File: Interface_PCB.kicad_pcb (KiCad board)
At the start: 2 copper layers, 46.5 x 47.9 mm, 48 parts, among them IC1 STM32L412RBT6P, J1 Conn_01x04, J2 Conn_01x04, J3 Conn_01x04, J4 Conn_01x04, J5 AVR-JTAG-10, J6 Micro_SD_Card, J7 USB_B, J8 Conn_01x02_Male, U1 AMS1117-3.3, Y1 Crystal, Y2 Crystal

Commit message: Design 5.0
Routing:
- net LSE_OUT: track 13.5 -> 15.1 mm, vias 2 -> 0
- net GND: track 86.6 -> 87.6 mm
- net LSE_IN: track 9.17 -> 8.66 mm
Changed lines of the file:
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@@
     (property "Sheetname" "")
     (attr smd)
-    (fp_text reference "Cl2" (at -1.5702 1.0562 180) (layer "F.SilkS")
+    (fp_text reference "Cl2" (at -1.498 0.7768 180) (layer "F.SilkS")
       (effects (font (size 0.5 0.5) (thickness 0.125)))
     )
@@
   (segment (start 132.3256 111.1334) (end 131.8556 111.6034) (width 0.25) (layer "F.Cu") (net 2))
   (segment (start 126.5556 100.0236) (end 124.7756 100.0236) (width 0.25) (layer "F.Cu") (net 2))
-  (segment (start 126.7743 109.5248) (end 125.9738 109.5248) (width 0.25) (layer "F.Cu") (net 2))
-  (segment (start 125.768 96.611) (end 127.308 96.611) (width 0.25) (layer "F.Cu") (net 2))
   (segment (start 125.8502 103.5236) (end 125.8316 103.505) (width 0.25) (layer "F.Cu") (net 2))
   (segment (start 132.8674 93.8754) (end 132.7856 93.7936) (width 0.25) (layer "F.Cu") (net 2))
+  (segment (start 126.5428 96.5962) (end 126.5576 96.611) (width 0.25) (layer "F.Cu") (net 2))
   (segment (start 132.386 105.859668) (end 132.386 108.7604) (width 0.25) (layer "F.Cu") (net 2))
   (segment (start 129.898 104.7724) (end 131.5948 104.7724) (width 0.25) (layer "F.Cu") (net 2))
+  (segment (start 125.7828 96.5962) (end 125.768 96.611) (width 0.25) (layer "F.Cu") (net 2))
   (segment (start 128.4224 115.3008) (end 130.0328 113.6904) (width 0.25) (layer "F.Cu") (net 2))
-  (segment (start 125.768 96.611) (end 125.768 96.596) (width 0.25) (layer "F.Cu") (net 2))
   (segment (start 143.3056 99.5236) (end 145.2756 99.5236) (width 0.25) (layer "F.Cu") (net 2))
   (segment (start 132.7856 92.2636) (end 133.2556 91.7936) (width 0.25) (layer "F.Cu") (net 2))
@@
   (segment (start 138.9229 85.9028) (end 137.8979 85.9028) (width 0.25) (layer "F.Cu") (net 2))
   (segment (start 152.3977 92.8878) (end 152.3977 89.2302) (width 0.25) (layer "F.Cu") (net 2))
-  (segment (start 125.768 96.596) (end 126.4864 95.8776) (width 0.25) (layer "F.Cu") (net 2))
   (segment (start 152.3977 92.8878) (end 154.0764 92.8878) (width 0.25) (layer "F.Cu") (net 2))
   (segment (start 154.0764 92.8878) (end 154.4066 92.5576) (width 0.25) (layer "F.Cu") (net 2))
+  (segment (start 126.5428 96.5962) (end 125.7828 96.5962) (width 0.25) (layer "F.Cu") (net 2))
   (segment (start 138.3792 121.7676) (end 138.3556 121.744) (width 0.25) (layer "F.Cu") (net 2))
   (segment (start 132.585896 105.659772) (end 132.386 105.859668) (width 0.25) (layer "F.Cu") (net 2))
@@
   (segment (start 141.374 99.7724) (end 143.0568 99.7724) (width 0.25) (layer "F.Cu") (net 2))
   (segment (start 117.5202 117.4186) (end 117.4242 117.3226) (width 0.25) (layer "F.Cu") (net 2))
+  (segment (start 125.3744 107.7696) (end 125.3744 108.9254) (width 0.25) (layer "F.Cu") (net 2))
   (segment (start 130.9588 113.6904) (end 131.8556 112.7936) (width 0.25) (layer "F.Cu") (net 2))
   (segment (start 132.386 98.1468) (end 133.4008 99.1616) (width 0.25) (layer "F.Cu") (net 2))
@@
   (segment (start 152.6006 122.2476) (end 152.4254 122.0724) (width 0.25) (layer "F.Cu") (net 2))
   (segment (start 125.3744 115.3008) (end 128.4224 115.3008) (width 0.25) (layer "F.Cu") (net 2))
+  (segment (start 125.3744 108.9254) (end 125.9738 109.5248) (width 0.25) (layer "F.Cu") (net 2))
   (segment (start 132.386 96.214) (end 132.8674 95.7326) (width 0.25) (layer "F.Cu") (net 2))
   (segment (start 148.844 114.681) (end 148.6014 114.4384) (width 0.25) (layer "F.Cu") (net 2))
   (segment (start 124.7756 100.0236) (end 124.5556 100.2436) (width 0.25) (layer "F.Cu") (net 2))
   (segment (start 138.886 108.7604) (end 138.886 107.7229) (width 0.25) (layer "F.Cu") (net 2))
+  (segment (start 126.7235 109.5248) (end 125.9738 109.5248) (width 0.25) (layer "F.Cu") (net 2))
   (segment (start 123.2566 117.4186) (end 125.3744 115.3008) (width 0.25) (layer "F.Cu") (net 2))
+  (segment (start 126.7743 109.474) (end 126.7235 109.5248) (width 0.25) (layer "F.Cu") (net 2))
   (segment (start 148.6014 114.4384) (end 147.1418 114.4384) (width 0.25) (layer "F.Cu") (net 2))
   (segment (start 124.5108 99.4431) (end 124.5556 99.4879) (width 0.25) (layer "F.Cu") (net 2))
   (segment (start 149.6594 112.4966) (end 149.6594 112.8294) (width 0.25) (layer "F.Cu") (net 2))
   (segment (start 138.9229 90.9828) (end 139.6179 90.2878) (width 0.25) (layer "F.Cu") (net 2))
+  (segment (start 126.5576 96.611) (end 127.308 96.611) (width 0.25) (layer "F.Cu") (net 2))
   (segment (start 151.8718 125.5216) (end 152.8572 124.5362) (width 0.25) (layer "F.Cu") (net 2))
   (via (at 152.4254 122.0724) (size 0.8) (drill 0.4) (layers "F.Cu" "B.Cu") (net 2))
@@
   (via (at 138.3792 121.7676) (size 0.8) (drill 0.4) (layers "F.Cu" "B.Cu") (net 2))
   (via (at 157.226 116.332) (size 0.8) (drill 0.4) (layers "F.Cu" "B.Cu") (net 2))
-  (via (at 126.4864 95.8776) (size 0.8) (drill 0.4) (layers "F.Cu" "B.Cu") (net 2))
+  (via (at 126.5428 96.5962) (size 0.8) (drill 0.4) (layers "F.Cu" "B.Cu") (net 2))
   (via (at 124.5108 99.4431) (size 0.8) (drill 0.4) (layers "F.Cu" "B.Cu") (net 2))
   (via (at 132.585896 105.659772) (size 0.8) (drill 0.4) (layers "F.Cu" "B.Cu") (net 2))
   (via (at 145.0848 113.03) (size 0.8) (drill 0.4) (layers "F.Cu" "B.Cu") (net 2))
   (via (at 138.4808 106.3498) (size 0.8) (drill 0.4) (layers "F.Cu" "B.Cu") (net 2))
-  (via (at 126.7743 109.5248) (size 0.8) (drill 0.4) (layers "F.Cu" "B.Cu") (net 2))
+  (via (at 126.7743 109.474) (size 0.8) (drill 0.4) (layers "F.Cu" "B.Cu") (net 2))
   (via (at 151.0792 114.2492) (size 0.8) (drill 0.4) (layers "F.Cu" "B.Cu") (net 2))
   (via (at 117.4242 117.3226) (size 0.8) (drill 0.4) (layers "F.Cu" "B.Cu") (net 2))
@@
   (segment (start 127.8738 109.5248) (end 127.8738 106.2591) (width 0.25) (layer "F.Cu") (net 4))
   (segment (start 127.8738 106.2591) (end 128.8605 105.2724) (width 0.25) (layer "F.Cu") (net 4))
-  (segment (start 130.9605 100.2474) (end 130.9605 98.083595) (width 0.25) (layer "F.Cu") (net 5))
-  (segment (start 128.268 95.291) (end 127.338 94.361) (width 0.25) (layer "F.Cu") (net 5))
+  (segment (start 128.615 96.611) (end 128.268 96.611) (width 0.25) (layer "F.Cu") (net 5))
   (segment (start 130.9355 100.2724) (end 130.9605 100.2474) (width 0.25) (layer "F.Cu") (net 5))
-  (segment (start 130.9605 98.083595) (end 129.487905 96.611) (width 0.25) (layer "F.Cu") (net 5))
-  (segment (start 129.898 100.2724) (end 130.9355 100.2724) (width 0.25) (layer "F.Cu") (net 5))
+  (segment (start 128.268 95.291) (end 127.338 94.361) (width 0.25) (layer "F.Cu") (net 5))
+  (segment (start 130.9605 100.2474) (end 130.9605 98.9565) (width 0.25) (layer "F.Cu") (net 5))
+  (segment (start 130.9605 98.9565) (end 128.615 96.611) (width 0.25) (layer "F.Cu") (net 5))
   (segment (start 128.268 96.611) (end 128.268 95.291) (width 0.25) (layer "F.Cu") (net 5))
-  (segment (start 129.487905 96.611) (end 128.268 96.611) (width 0.25) (layer "F.Cu") (net 5))
-  (segment (start 124.808 95.791) (end 126.238 94.361) (width 0.25) (layer "F.Cu") (net 6))
-  (segment (start 131.071896 100.7724) (end 131.685 100.159296) (width 0.25) (layer "F.Cu") (net 6))
-  (segment (start 124.808 96.618609) (end 124.808 96.611) (width 0.25) (layer "F.Cu") (net 6))
-  (segment (start 130.048 98.1964) (end 126.385791 98.1964) (width 0.25) (layer "F.Cu") (net 6))
-  (segment (start 124.808 96.611) (end 124.808 95.791) (width 0.25) (layer "F.Cu") (net 6))
-  (segment (start 126.385791 98.1964) (end 124.808 96.618609) (width 0.25) (layer "F.Cu") (net 6))
-  (segment (start 129.898 100.7724) (end 131.071896 100.7724) (width 0.25) (layer "F.Cu") (net 6))
-  (segment (start 124.7338 96.6852) (end 124.808 96.611) (width 0.25) (layer "F.Cu") (net 6))
-  (segment (start 131.685 100.159296) (end 131.685 100.1014) (width 0.25) (layer "F.Cu") (net 6))
-  (via (at 131.685 100.1014) (size 0.8) (drill 0.4) (layers "F.Cu" "B.Cu") (net 6))
-  (via (at 130.048 98.1964) (size 0.8) (drill 0.4) (layers "F.Cu" "B.Cu") (net 6))
-  (segment (start 131.685 100.1014) (end 131.685 99.8334) (width 0.25) (layer "B.Cu") (net 6))
-  (segment (start 131.685 99.8334) (end 130.048 98.1964) (width 0.25) (layer "B.Cu") (net 6))
+  (segment (start 129.898 100.2724) (end 130.9355 100.2724) (width 0.25) (layer "F.Cu") (net 5))
+  (segment (start 126.238 94.361) (end 124.808 95.791) (width 0.25) (layer "F.Cu") (net 6))
+  (segment (start 131.411 100.433296) (end 131.071896 100.7724) (width 0.25) (layer "F.Cu") (net 6))
+  (segment (start 131.411 96.994) (end 131.411 100.433296) (width 0.25) (layer "F.Cu") (net 6))
+  (segment (start 131.071896 100.7724) (end 129.898 100.7724) (width 0.25) (layer "F.Cu") (net 6))
+  (segment (start 131.411 96.994) (end 127.953 93.536) (width 0.25) (layer "F.Cu") (net 6))
+  (segment (start 126.238 93.9038) (end 126.238 94.361) (width 0.25) (layer "F.Cu") (net 6))
+  (segment (start 124.808 95.791) (end 124.808 96.611) (width 0.25) (layer "F.Cu") (net 6))
+  (segment (start 127.953 93.536) (end 126.6058 93.536) (width 0.25) (layer "F.Cu") (net 6))
+  (segment (start 126.6058 93.536) (end 126.238 93.9038) (width 0.25) (layer "F.Cu") (net 6))
   (segment (start 121.92 107.2822) (end 122.3926 106.8096) (width 0.25) (layer "F.Cu") (net 7))
-  (segment (start 126.7644 106.8096) (end 126.8056 106.7684) (width 0.25) (layer "F.Cu") (net 7))
-  (segment (start 126.7162 106.8578) (end 126.8056 106.7684) (width 0.25) (layer "F.Cu") (net 7))
   (segment (start 125.3744 106.8096) (end 126.7644 106.8096) (width 0.25) (layer "F.Cu") (net 7))
   (segment (start 122.3926 106.8096) (end 125.3744 106.8096) (width 0.25) (layer "F.Cu") (net 7))

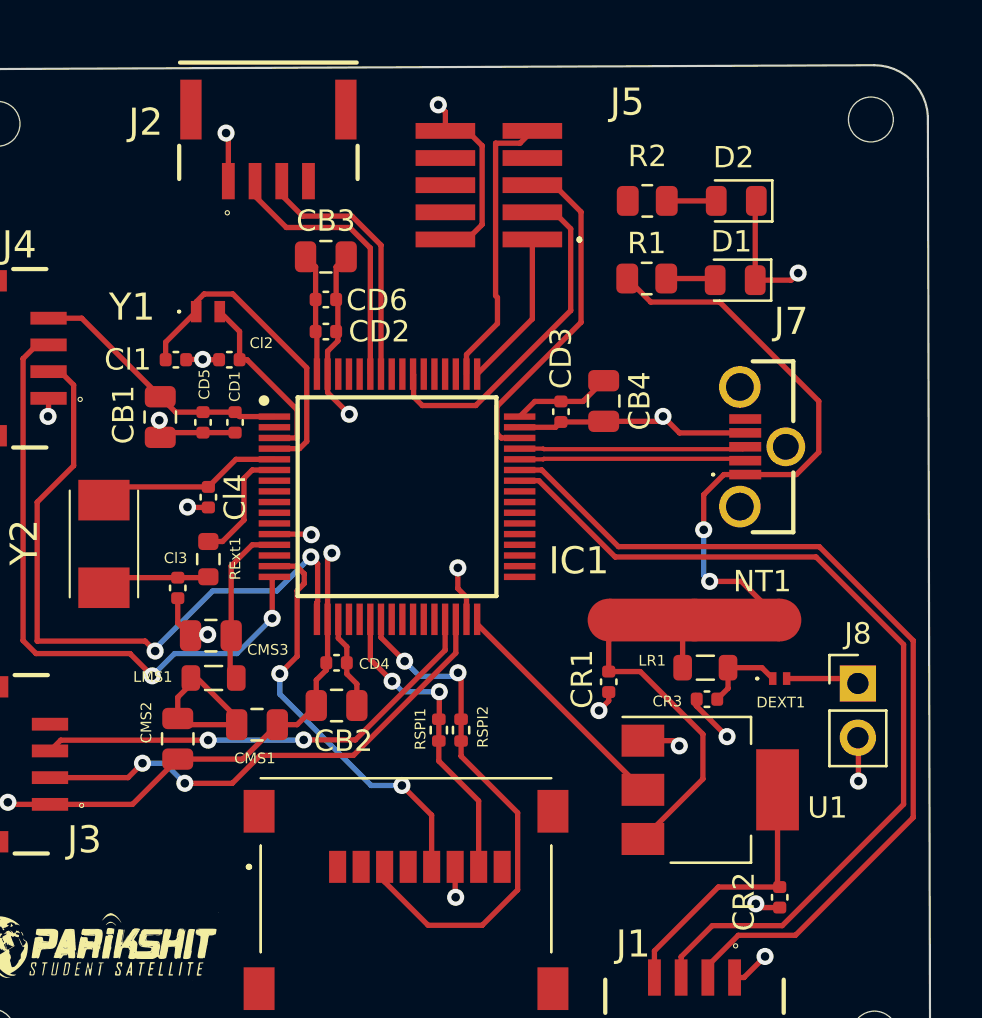
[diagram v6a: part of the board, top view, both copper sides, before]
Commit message: Updated inductor and USB according to manufacturer
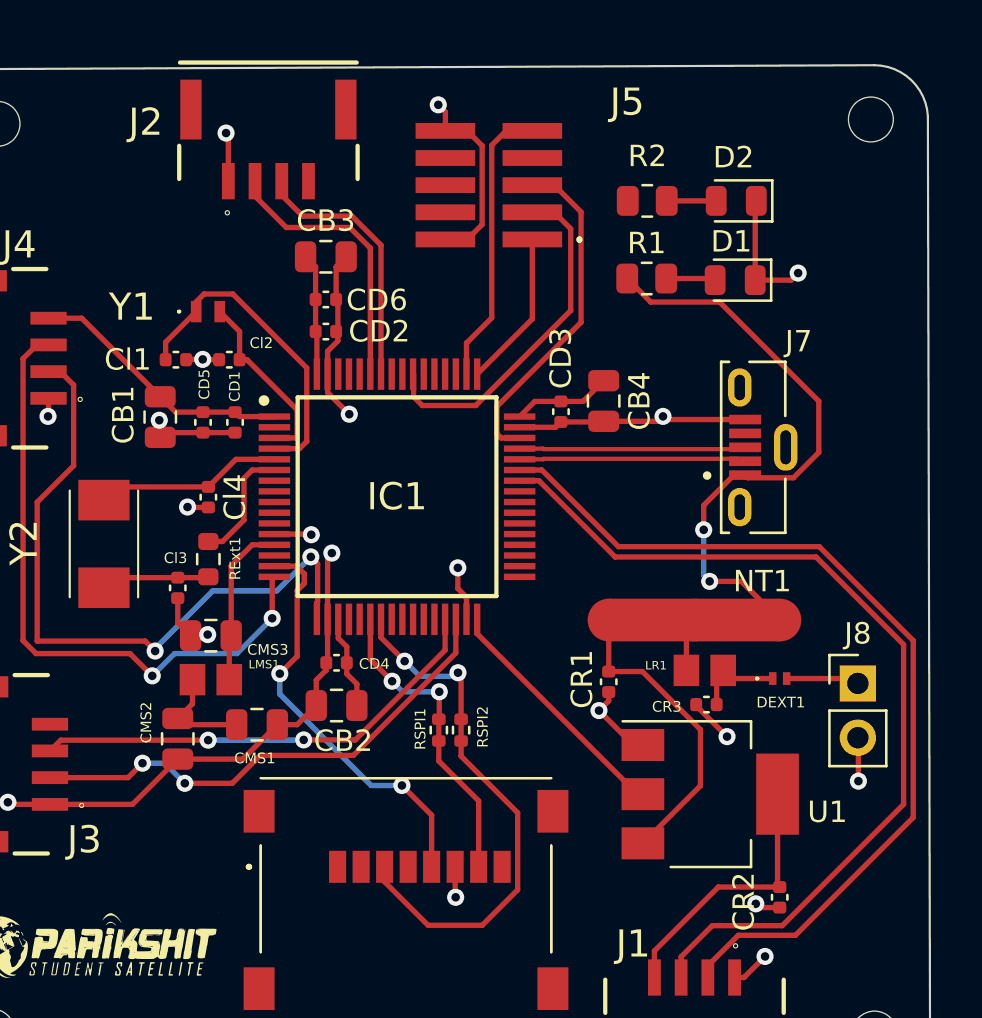
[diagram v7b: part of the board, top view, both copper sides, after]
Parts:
- J7: value USB_B -> GMCB05B11124H1EU; footprint SamacSys_Parts:GMCB05B11124H1EU -> GMCB05B11124H1EU (1):AMPHENOL_GMCB05B11124H1EU
- LMS1, LR1: value 39nH -> AIMC-0805-39NJ-T; footprint Inductor_SMD:L_0805_2012Metric -> AIMC-0805-39NJ-T:INDC2012X105N
- moved J7 1.00 mm to (151.7, 100.7)
- moved CR3 0.26 mm to (150.1, 112.8)
- moved U1 0.20 mm to (150.3, 116.9)
- moved LMS1 0.15 mm to (126.9, 111.6)
- moved LR1 0.13 mm to (150.0, 111.2)
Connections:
- J7 pad 4: GND -> unconnected-(J7-Pad4)
- J7 pad 5: unconnected-(J7-Pad5) -> GND
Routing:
- net +3V3: track 60.0 -> 57.3 mm
- net Net-(NT1-Pad2): track 2.46 -> 3.30 mm
- net GND: vias 21 -> 20
